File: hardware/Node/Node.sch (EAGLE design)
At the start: 67 parts, among them J1 AVR_SPI_PRG_6NS, J2 M04X2, Q1 PMR280UN, Q2 PMR280UN, Q3 PMR280UN, SW1 KSS, SW2 KSS, U1 ATMEGA32U4QFN, U2 BLUETOOTH-RN41", U3 LSM303DLM, U4 L3GD20, U5 8.0MHz, U6 MCP73871, U7 V_REG_LDOSMD, U9 RCLAMP0502A, X1 USBSMD

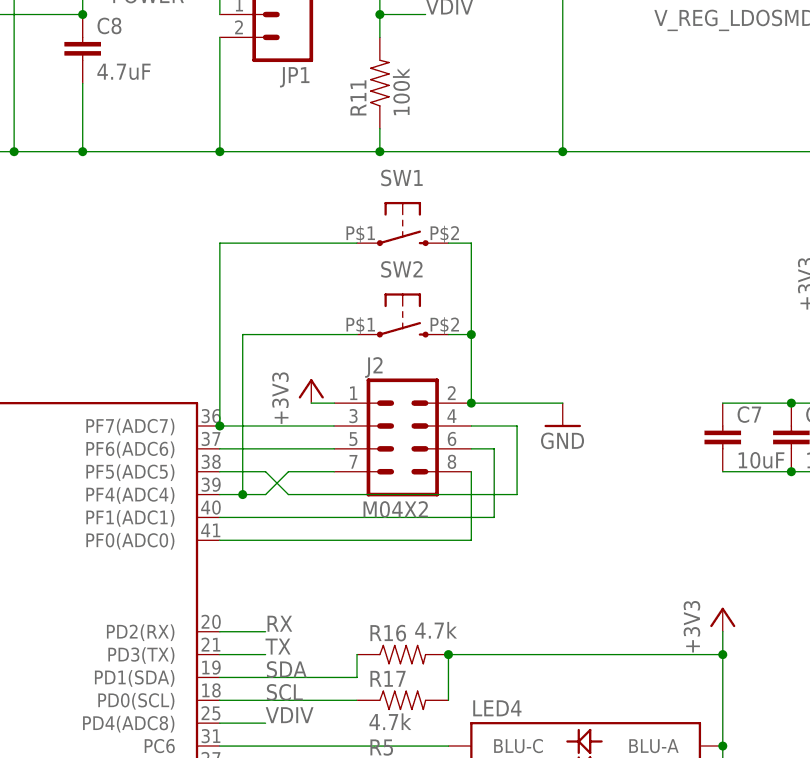
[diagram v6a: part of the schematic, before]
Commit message: reorder some pins
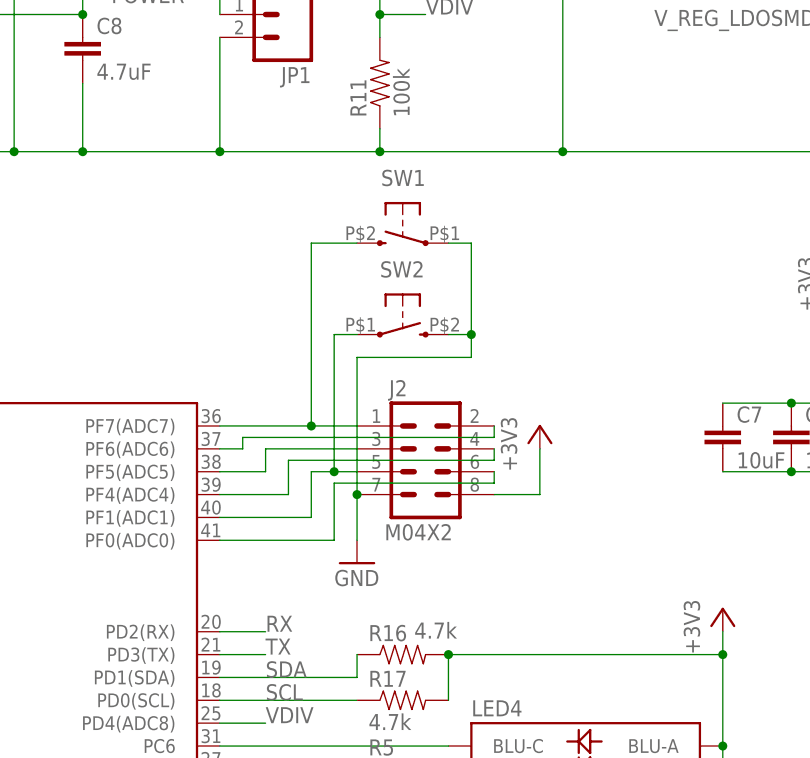
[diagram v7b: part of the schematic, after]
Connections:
- removed net N$15: J2.4, U1.PF5(ADC5)
- new net N$33: J2.4, U1.PF4(ADC4)
- net +3V3: now also J2.8; no longer J2.1
- net GND: now also J2.7, SW1.1; no longer J2.2, SW1.3
- net N$28: now also J2.1, SW1.3; no longer J2.3, SW1.1
- net N$30: now also J2.2, U1.PF6(ADC6); no longer J2.7, SW2.1, U1.PF4(ADC4)
- net N$32: now also J2.3, U1.PF5(ADC5); no longer J2.5, U1.PF6(ADC6)
- net N$34: now also J2.5, SW2.1; no longer J2.6
- net N$35: now also J2.6; no longer J2.8
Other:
- moved on the sheet: J2
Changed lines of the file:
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@@
 <setting verticaltext="up"/>
 </settings>
-<grid distance="0.1" unitdist="inch" unit="inch" style="lines" multiple="1" display="no" altdistance="0.01" altunitdist="inch" altunit="inch"/>
+<grid distance="0.1" unitdist="inch" unit="inch" style="lines" multiple="1" display="no" altdistance="0.05" altunitdist="inch" altunit="inch"/>
 <layers>
 <layer number="1" name="Top" color="4" fill="1" visible="no" active="no"/>
@@
 <instance part="R9" gate="G$1" x="73.66" y="96.52"/>
 <instance part="GND7" gate="1" x="33.02" y="91.44"/>
-<instance part="SW1" gate="G$1" x="160.02" y="154.94"/>
+<instance part="SW1" gate="G$1" x="160.02" y="154.94" rot="MR0"/>
 <instance part="SW2" gate="G$1" x="160.02" y="144.78"/>
 <instance part="HWB" gate="G$1" x="48.26" y="134.62" smashed="yes">
@@
 <instance part="R3" gate="G$1" x="48.26" y="162.56" rot="R90"/>
 <instance part="R19" gate="G$1" x="55.88" y="162.56" rot="R90"/>
-<instance part="GND9" gate="1" x="177.8" y="134.62"/>
+<instance part="GND9" gate="1" x="154.94" y="119.38"/>
 <instance part="LED1" gate="G$1" x="50.8" y="203.2"/>
 <instance part="R20" gate="G$1" x="50.8" y="193.04" rot="R90"/>
 <instance part="R10" gate="G$1" x="157.48" y="187.96" rot="R90"/>
 <instance part="R11" gate="G$1" x="157.48" y="172.72" rot="R90"/>
-<instance part="J2" gate="G$1" x="160.02" y="132.08"/>
-<instance part="+3V9" gate="G$1" x="149.86" y="139.7"/>
+<instance part="J2" gate="G$1" x="162.56" y="129.54"/>
+<instance part="+3V9" gate="G$1" x="175.26" y="134.62"/>
 <instance part="JP2" gate="G$1" x="147.32" y="22.86" rot="R180"/>
 </instances>
@@
 </segment>
 <segment>
+<pinref part="GND9" gate="1" pin="GND"/>
+<pinref part="J2" gate="G$1" pin="7"/>
+<wire x1="154.94" y1="121.92" x2="154.94" y2="127" width="0.1524" layer="91"/>
 <pinref part="SW2" gate="G$1" pin="3"/>
 <wire x1="165.1" y1="144.78" x2="167.64" y2="144.78" width="0.1524" layer="91"/>
-<pinref part="J2" gate="G$1" pin="2"/>
-<wire x1="167.64" y1="137.16" x2="167.64" y2="144.78" width="0.1524" layer="91"/>
+<wire x1="167.64" y1="154.94" x2="167.64" y2="144.78" width="0.1524" layer="91"/>
+<wire x1="167.64" y1="144.78" x2="167.64" y2="142.24" width="0.1524" layer="91"/>
+<wire x1="167.64" y1="142.24" x2="154.94" y2="142.24" width="0.1524" layer="91"/>
 <junction x="167.64" y="144.78"/>
-<pinref part="SW1" gate="G$1" pin="3"/>
-<wire x1="165.1" y1="154.94" x2="167.64" y2="154.94" width="0.1524" layer="91"/>
-<wire x1="167.64" y1="154.94" x2="167.64" y2="144.78" width="0.1524" layer="91"/>
-<pinref part="GND9" gate="1" pin="GND"/>
-<wire x1="167.64" y1="137.16" x2="177.8" y2="137.16" width="0.1524" layer="91"/>
-<junction x="167.64" y="137.16"/>
+<wire x1="154.94" y1="142.24" x2="154.94" y2="127" width="0.1524" layer="91"/>
+<junction x="154.94" y="127"/>
+<pinref part="SW1" gate="G$1" pin="1"/>
+<wire x1="167.64" y1="154.94" x2="165.1" y2="154.94" width="0.1524" layer="91"/>
 </segment>
 </net>
@@
 </segment>
 <segment>
+<pinref part="J2" gate="G$1" pin="8"/>
+<wire x1="170.18" y1="127" x2="175.26" y2="127" width="0.1524" layer="91"/>
 <pinref part="+3V9" gate="G$1" pin="+3V3"/>
-<pinref part="J2" gate="G$1" pin="1"/>
-<wire x1="149.86" y1="137.16" x2="152.4" y2="137.16" width="0.1524" layer="91"/>
+<wire x1="175.26" y1="127" x2="175.26" y2="132.08" width="0.1524" layer="91"/>
 </segment>
 </net>
@@
 </segment>
 </net>
-<net name="N$28" class="0">
-<segment>
-<pinref part="U1" gate="G$1" pin="PF7(ADC7)"/>
-<wire x1="139.7" y1="134.62" x2="152.4" y2="134.62" width="0.1524" layer="91"/>
-<pinref part="SW1" gate="G$1" pin="1"/>
-<wire x1="154.94" y1="154.94" x2="139.7" y2="154.94" width="0.1524" layer="91"/>
-<wire x1="139.7" y1="154.94" x2="139.7" y2="134.62" width="0.1524" layer="91"/>
-<junction x="139.7" y="134.62"/>
-<pinref part="J2" gate="G$1" pin="3"/>
-</segment>
-</net>
-<net name="N$34" class="0">
-<segment>
-<pinref part="U1" gate="G$1" pin="PF1(ADC1)"/>
-<wire x1="139.7" y1="124.46" x2="170.18" y2="124.46" width="0.1524" layer="91"/>
-<wire x1="170.18" y1="124.46" x2="170.18" y2="132.08" width="0.1524" layer="91"/>
-<wire x1="170.18" y1="132.08" x2="167.64" y2="132.08" width="0.1524" layer="91"/>
-<pinref part="J2" gate="G$1" pin="6"/>
-</segment>
-</net>
-<net name="N$35" class="0">
-<segment>
-<pinref part="U1" gate="G$1" pin="PF0(ADC0)"/>
-<wire x1="139.7" y1="121.92" x2="167.64" y2="121.92" width="0.1524" layer="91"/>
-<wire x1="167.64" y1="121.92" x2="167.64" y2="129.54" width="0.1524" layer="91"/>
-<pinref part="J2" gate="G$1" pin="8"/>
-</segment>
-</net>
 <net name="RX_I" class="0">
 <segment>
@@
 </segment>
 </net>
-<net name="N$15" class="0">
+<net name="N$28" class="0">
+<segment>
+<pinref part="U1" gate="G$1" pin="PF7(ADC7)"/>
+<pinref part="J2" gate="G$1" pin="1"/>
+<wire x1="139.7" y1="134.62" x2="149.86" y2="134.62" width="0.1524" layer="91"/>
+<wire x1="149.86" y1="134.62" x2="154.94" y2="134.62" width="0.1524" layer="91"/>
+<wire x1="149.86" y1="154.94" x2="149.86" y2="134.62" width="0.1524" layer="91"/>
+<junction x="149.86" y="134.62"/>
+<pinref part="SW1" gate="G$1" pin="3"/>
+<wire x1="149.86" y1="154.94" x2="154.94" y2="154.94" width="0.1524" layer="91"/>
+</segment>
+</net>
+<net name="N$30" class="0">
+<segment>
+<pinref part="U1" gate="G$1" pin="PF6(ADC6)"/>
+<wire x1="139.7" y1="132.08" x2="142.24" y2="132.08" width="0.1524" layer="91"/>
+<wire x1="142.24" y1="132.08" x2="142.24" y2="133.35" width="0.1524" layer="91"/>
+<wire x1="142.24" y1="133.35" x2="170.18" y2="133.35" width="0.1524" layer="91"/>
+<pinref part="J2" gate="G$1" pin="2"/>
+<wire x1="170.18" y1="133.35" x2="170.18" y2="134.62" width="0.1524" layer="91"/>
+</segment>
+</net>
+<net name="N$32" class="0">
 <segment>
 <pinref part="U1" gate="G$1" pin="PF5(ADC5)"/>
 <wire x1="139.7" y1="129.54" x2="144.78" y2="129.54" width="0.1524" layer="91"/>
-<wire x1="172.72" y1="127" x2="172.72" y2="134.62" width="0.1524" layer="91"/>
-<wire x1="172.72" y1="134.62" x2="167.64" y2="134.62" width="0.1524" layer="91"/>
+<pinref part="J2" gate="G$1" pin="3"/>
+<wire x1="144.78" y1="129.54" x2="144.78" y2="132.08" width="0.1524" layer="91"/>
+<wire x1="144.78" y1="132.08" x2="154.94" y2="132.08" width="0.1524" layer="91"/>
+</segment>
+</net>
+<net name="N$33" class="0">
+<segment>
+<pinref part="U1" gate="G$1" pin="PF4(ADC4)"/>
+<wire x1="139.7" y1="127" x2="147.32" y2="127" width="0.1524" layer="91"/>
+<wire x1="147.32" y1="127" x2="147.32" y2="130.81" width="0.1524" layer="91"/>
+<wire x1="147.32" y1="130.81" x2="170.18" y2="130.81" width="0.1524" layer="91"/>
 <pinref part="J2" gate="G$1" pin="4"/>
-<wire x1="144.78" y1="129.54" x2="147.32" y2="127" width="0.1524" layer="91"/>
-<wire x1="147.32" y1="127" x2="172.72" y2="127" width="0.1524" layer="91"/>
-</segment>
-</net>
-<net name="N$32" class="0">
-<segment>
+<wire x1="170.18" y1="130.81" x2="170.18" y2="132.08" width="0.1524" layer="91"/>
+</segment>
+</net>
+<net name="N$34" class="0">
+<segment>
+<pinref part="U1" gate="G$1" pin="PF1(ADC1)"/>
+<wire x1="139.7" y1="124.46" x2="149.86" y2="124.46" width="0.1524" layer="91"/>
 <pinref part="J2" gate="G$1" pin="5"/>
-<pinref part="U1" gate="G$1" pin="PF6(ADC6)"/>
-<wire x1="139.7" y1="132.08" x2="152.4" y2="132.08" width="0.1524" layer="91"/>
-</segment>
-</net>
-<net name="N$30" class="0">
-<segment>
+<wire x1="149.86" y1="124.46" x2="149.86" y2="129.54" width="0.1524" layer="91"/>
+<wire x1="149.86" y1="129.54" x2="152.4" y2="129.54" width="0.1524" layer="91"/>
 <pinref part="SW2" gate="G$1" pin="1"/>
-<wire x1="154.94" y1="144.78" x2="142.24" y2="144.78" width="0.1524" layer="91"/>
-<pinref part="U1" gate="G$1" pin="PF4(ADC4)"/>
-<wire x1="139.7" y1="127" x2="142.24" y2="127" width="0.1524" layer="91"/>
-<pinref part="J2" gate="G$1" pin="7"/>
-<wire x1="142.24" y1="127" x2="144.78" y2="127" width="0.1524" layer="91"/>
-<wire x1="144.78" y1="127" x2="147.32" y2="129.54" width="0.1524" layer="91"/>
-<wire x1="147.32" y1="129.54" x2="152.4" y2="129.54" width="0.1524" layer="91"/>
-<wire x1="142.24" y1="144.78" x2="142.24" y2="127" width="0.1524" layer="91"/>
-<junction x="142.24" y="127"/>
-</segment>
-</net>
+<wire x1="152.4" y1="129.54" x2="154.94" y2="129.54" width="0.1524" layer="91"/>
+<wire x1="154.94" y1="144.78" x2="152.4" y2="144.78" width="0.1524" layer="91"/>
+<wire x1="152.4" y1="144.78" x2="152.4" y2="129.54" width="0.1524" layer="91"/>
+<junction x="152.4" y="129.54"/>
+</segment>
+</net>
+<net name="N$35" class="0">
+<segment>
+<pinref part="U1" gate="G$1" pin="PF0(ADC0)"/>
+<wire x1="139.7" y1="121.92" x2="152.4" y2="121.92" width="0.1524" layer="91"/>
+<wire x1="152.4" y1="121.92" x2="152.4" y2="128.27" width="0.1524" layer="91"/>
+<wire x1="152.4" y1="128.27" x2="170.18" y2="128.27" width="0.1524" layer="91"/>
+<pinref part="J2" gate="G$1" pin="6"/>
+<wire x1="170.18" y1="128.27" x2="170.18" y2="129.54" width="0.1524" layer="91"/>
+</segment>
+</net>
